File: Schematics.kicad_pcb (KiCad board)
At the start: 2 copper layers, 73 parts, among them Q1 AO3400A, Q2 SI2301CDS-T1-E3, Q3 SI2301CDS-T1-E3, Q4 8050, U2 CAT24C32, U3 ME6217C33M5G, U6 TXB0108PWR

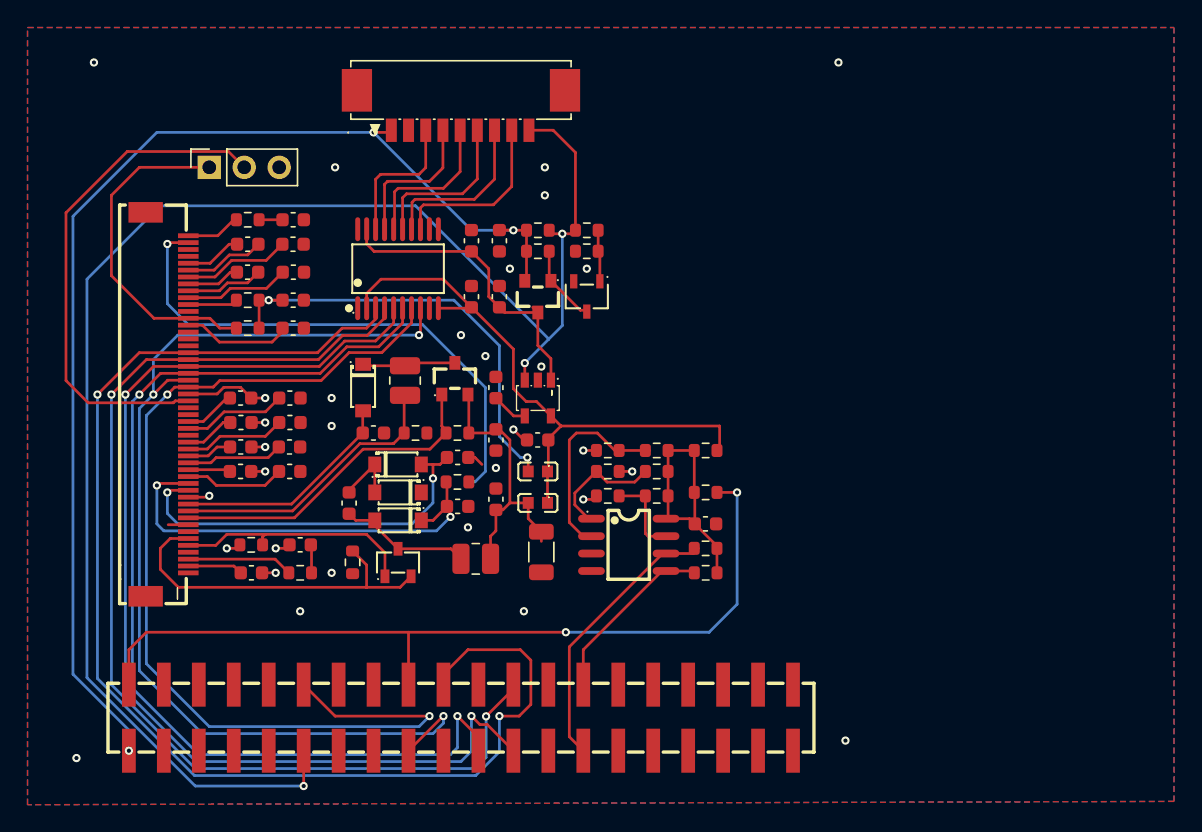
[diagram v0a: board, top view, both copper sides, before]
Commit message: made changes to simplify the board
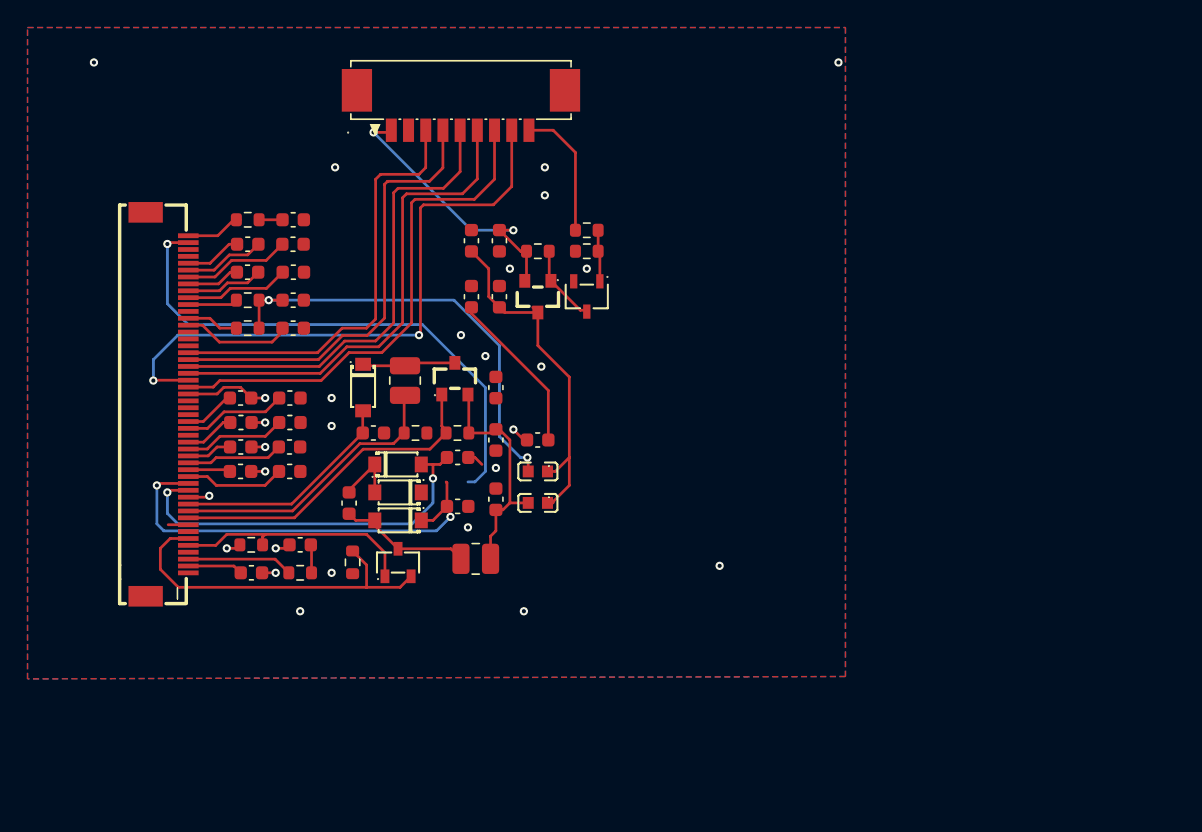
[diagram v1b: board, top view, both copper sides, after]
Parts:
- removed C23: 100nF/50V, Capacitor_SMD:C_0603_1608Metric
- removed C29: 100uF/6.3V, Capacitor_SMD:C_1206_3216Metric
- removed J2: ~, Connector_PinSocket_2.54mm:PinSocket_1x03_P2.54mm_Vertical
- removed R1, R16, R17, R19: 0R, Resistor_SMD:R_0603_1608Metric
- removed R10, R14, R18, R9: NC, Resistor_SMD:R_0603_1608Metric
- removed R12: 1K, Resistor_SMD:R_0603_1608Metric
- removed R13, R15: 3.9KΩ, Resistor_SMD:R_0603_1608Metric
- removed R7: NC/47K, Resistor_SMD:R_0603_1608Metric
- removed U2: CAT24C32, local:SOIC-8_L5.0-W4.0-P1.27-LS6.0-BL
- removed U3: ME6217C33M5G, local:SOT-23-5_L3.0-W1.7-P0.95-LS2.8-BR
- removed U6: TXB0108PWR, local:TSSOP-20_L6.5-W4.4-P0.65-LS6.4-BL
- removed UP1: ~, local:HDR-SMD_40P-P2.54-V-F-R2-C20-S2.54-LS7.1
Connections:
- net /RPI_5V renamed /VCC_INT
- net VDD renamed /VDD
- J1 pad 26: /BS0 -> GND
- J1 pad 28: /EPD_RST' -> /EPD_RST
- J1 pad 29: /EPD_BUSY' -> /EPD_BUSY
- J1 pad 30: /EPD_DC' -> /EPD_DC
- J1 pad 31: /EPD_CS' -> /EPD_CS
- J1 pad 32: /EPD_SCK' -> /EPD_SCK
- J1 pad 33: /EPD_DIN' -> /EPD_DIN
- L3 pad 1: 3V3_OUT -> VCC
- L4 pad 1: 3V3_OUT -> VCC
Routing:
- net /PWR: track 113.9 -> 10.1 mm, vias 3 -> 0
- net /EPD_DIN': track 93.4 -> 0.00 mm, vias 2 -> 0
- net /EPD_SCK': track 80.3 -> 0.00 mm, vias 2 -> 0
- net /EPD_CS': track 78.5 -> 0.00 mm, vias 2 -> 0
- net /EPD_BUSY': track 76.4 -> 0.00 mm, vias 3 -> 0
- net /EPD_DC': track 75.2 -> 0.00 mm, vias 2 -> 0
- net /EPD_RST': track 74.0 -> 0.00 mm, vias 2 -> 0
- net /VCC_INT: track 85.1 -> 20.3 mm, vias 3 -> 2
- net /RPI_3V3: track 61.3 -> 0.00 mm, vias 2 -> 0
- net /BS0: track 37.1 -> 0.00 mm
- net /EPD_BUSY: track 12.9 -> 44.8 mm, vias 0 -> 2
- net 3V3_OUT: track 43.6 -> 12.0 mm
- net /EPD_RST: track 12.2 -> 37.2 mm
- net /EPD_DC: track 11.8 -> 35.7 mm
- net /EPD_CS: track 11.1 -> 34.2 mm
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
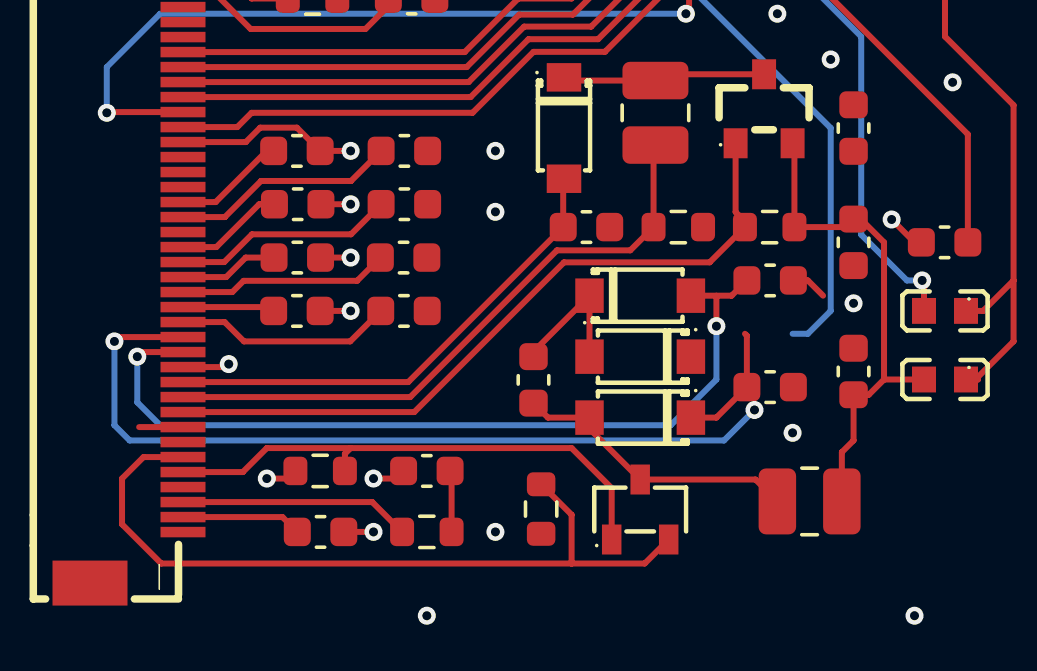
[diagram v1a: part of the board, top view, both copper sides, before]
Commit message: updated board by removing unnecessary elements
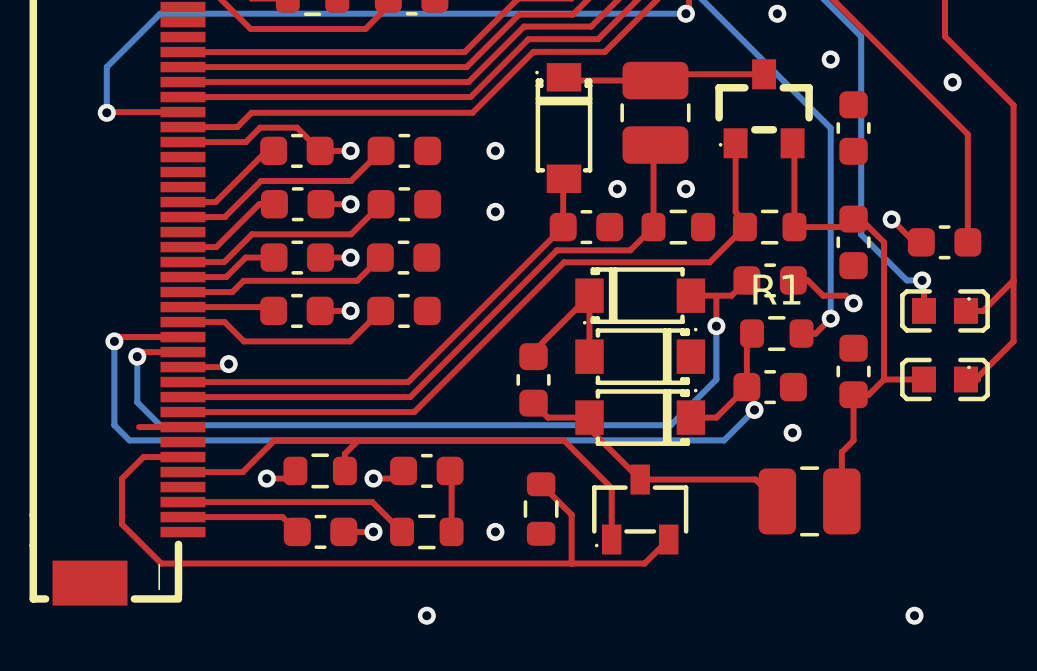
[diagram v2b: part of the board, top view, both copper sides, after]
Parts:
- added R1: 0R, Resistor_SMD:R_0603_1608Metric, F.Cu at (80.2, 66.5)
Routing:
- net GND: track 17.8 -> 18.9 mm, vias 27 -> 29
- net /GDRH: track 17.7 -> 18.3 mm
- net /VGH: track 39.2 -> 38.8 mm, vias 1 -> 2
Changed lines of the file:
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@@
 		)
 	)
+	(footprint "Resistor_SMD:R_0603_1608Metric"
+		(layer "F.Cu")
+		(at 80.245 66.541)
+		(descr "Resistor SMD 0603 (1608 Metric), square (rectangular) end terminal, IPC-7351 nominal, (Body size source: IPC-SM-782 page 72, https://www.pcb-3d.com/wordpress/wp-content/uploads/ipc-sm-782a_amendment_1_and_2.pdf)")
+		(tags "resistor")
+		(property "Reference" "R1"
+			(at 0 -1.43 0)
+			(layer "F.SilkS")
+			(effects
+				(font
+					(size 1 1)
+					(thickness 0.15)
+				)
+			)
+		)
+		(property "Value" "0R"
+			(at 0 1.43 0)
+			(layer "F.Fab")
+			(effects
+				(font
+					(size 1 1)
+					(thickness 0.15)
+				)
+			)
+		)
+		(property "Datasheet" ""
+			(at 0 0 0)
+			(layer "F.Fab")
+			(hide yes)
+			(effects
+				(font
+					(size 1.27 1.27)
+				)
+			)
+		)
+		(property "Description" "Resistor, small symbol"
+			(at 0 0 0)
+			(layer "F.Fab")
+			(hide yes)
+			(effects
+				(font
+					(size 1.27 1.27)
+				)
+			)
+		)
+		(property "KiLib_Generator" "SMD_2terminal_chip_molded"
+			(at 0 0 0)
+			(layer "F.SilkS")
+			(hide yes)
+			(effects
+				(font
+					(size 1 1)
+					(thickness 0.15)
+				)
+			)
+		)
+		(property ki_fp_filters "R_*")
+		(sheetname "/")
+		(sheetfile "Schematics.kicad_sch")
+		(units
+			(unit
+				(name "A")
+				(pins "1" "2")
+			)
+		)
+		(attr smd)
+		(duplicate_pad_numbers_are_jumpers no)
+		(fp_line
+			(start -0.237258 -0.5225)
+			(end 0.237258 -0.5225)
+			(stroke
+				(width 0.12)
+				(type solid)
+			)
+			(layer "F.SilkS")
+		)
+		(fp_line
+			(start -0.237258 0.5225)
+			(end 0.237258 0.5225)
+			(stroke
+				(width 0.12)
+				(type solid)
+			)
+			(layer "F.SilkS")
+		)
+		(fp_rect
+			(start -1.48 -0.73)
+			(end 1.48 0.73)
+			(stroke
+				(width 0.05)
+				(type solid)
+			)
+			(fill no)
+			(layer "F.CrtYd")
+		)
+		(fp_rect
+			(start -0.8 -0.4125)
+			(end 0.8 0.4125)
+			(stroke
+				(width 0.1)
+				(type solid)
+			)
+			(fill no)
+			(layer "F.Fab")
+		)
+		(fp_text user "${REFERENCE}"
+			(at 0 0 0)
+			(layer "F.Fab")
+			(effects
+				(font
+					(size 0.4 0.4)
+					(thickness 0.06)
+				)
+			)
+		)
+		(pad "1" smd roundrect
+			(at -0.825 0)
+			(size 0.8 0.95)
+			(layers "F.Cu" "F.Mask" "F.Paste")
+			(roundrect_rratio 0.25)
+			(net "/VPH")
+			(pintype "passive")
+		)
+		(pad "2" smd roundrect
+			(at 0.825 0)
+			(size 0.8 0.95)
+			(layers "F.Cu" "F.Mask" "F.Paste")
+			(roundrect_rratio 0.25)
+			(net "/VGH")
+			(pintype "passive")
+		)
+		(embedded_fonts no)
+		(model "${KICAD10_3DMODEL_DIR}/Resistor_SMD.3dshapes/R_0603_1608Metric.step"
+			(offset
+				(xyz 0 0 0)
+			)
+			(scale
+				(xyz 1 1 1)
+			)
+			(rotate
+				(xyz 0 0 0)
+			)
+		)
+	)
 	(footprint "local:SOD-123_L2.8-W1.8-LS3.7-RD"
 		(layer "F.Cu")
@@
 	)
 	(segment
+		(start 82.55 65.278)
+		(end 82.804 65.532)
+		(width 0.2)
+		(layer "F.Cu")
+		(net "GND")
+	)
+	(segment
 		(start 65.812 73.152)
 		(end 66.802 73.152)
@@
 	)
 	(segment
+		(start 81.788 65.278)
+		(end 82.55 65.278)
+		(width 0.2)
+		(layer "F.Cu")
+		(net "GND")
+	)
+	(segment
 		(start 67.551 71.374)
 		(end 67.805 71.12)
@@
 	)
 	(via
+		(at 74.93 61.722)
+		(size 0.6)
+		(drill 0.3)
+		(layers "F.Cu" "B.Cu")
+		(free yes)
+		(net "GND")
+	)
+	(via
 		(at 63.246 71.374)
 		(size 0.6)
@@
 	)
 	(via
+		(at 77.216 61.722)
+		(size 0.6)
+		(drill 0.3)
+		(layers "F.Cu" "B.Cu")
+		(free yes)
+		(net "GND")
+	)
+	(via
 		(at 86.106 58.166)
 		(size 0.6)
@@
 	)
 	(segment
-		(start 63.246 70.358)
-		(end 62.446 71.158)
+		(start 65.849 71.12)
+		(end 65.849 70.553)
 		(width 0.2)
 		(layer "F.Cu")
@@
 	)
 	(segment
-		(start 66.04 70.358)
-		(end 63.246 70.358)
+		(start 63.5 70.104)
+		(end 66.294 70.104)
 		(width 0.2)
 		(layer "F.Cu")
@@
 	)
 	(segment
-		(start 74.742 73.406)
-		(end 74.742 71.694)
+		(start 62.446 71.158)
+		(end 63.5 70.104)
 		(width 0.2)
 		(layer "F.Cu")
@@
 	)
 	(segment
-		(start 65.847 70.551)
-		(end 66.04 70.358)
+		(start 74.742 71.694)
+		(end 73.152 70.104)
 		(width 0.2)
 		(layer "F.Cu")
@@
 	)
 	(segment
-		(start 65.849 70.553)
-		(end 65.849 71.12)
+		(start 60.452 71.158)
+		(end 62.446 71.158)
 		(width 0.2)
 		(layer "F.Cu")
@@
 	)
 	(segment
-		(start 65.847 70.551)
-		(end 65.849 70.553)
+		(start 65.849 70.553)
+		(end 65.847 70.551)
 		(width 0.2)
 		(layer "F.Cu")
@@
 	)
 	(segment
-		(start 74.742 71.694)
-		(end 73.406 70.358)
+		(start 65.847 70.551)
+		(end 66.294 70.104)
 		(width 0.2)
 		(layer "F.Cu")
@@
 	)
 	(segment
-		(start 73.406 70.358)
-		(end 66.04 70.358)
+		(start 74.742 73.406)
+		(end 74.742 71.694)
 		(width 0.2)
 		(layer "F.Cu")
@@
 	)
 	(segment
-		(start 62.446 71.158)
-		(end 60.452 71.158)
+		(start 66.294 70.104)
+		(end 73.152 70.104)
 		(width 0.2)
 		(layer "F.Cu")
@@
 	)
 	(segment
+		(start 81.541 66.541)
+		(end 82.042 66.04)
+		(width 0.2)
+		(layer "F.Cu")
+		(net "/VGH")
+	)
+	(segment
 		(start 59.028 49.158)
 		(end 60.452 49.158)
@@
 		(net "/VGH")
 	)
+	(segment
+		(start 81.07 66.541)
+		(end 81.541 66.541)
+		(width 0.2)
+		(layer "F.Cu")
+		(net "/VGH")
+	)
+	(via
+		(at 82.042 66.04)
+		(size 0.6)
+		(drill 0.3)
+		(layers "F.Cu" "B.Cu")
+		(net "/VGH")
+	)
 	(via
 		(at 58.928 49.258)
@@
 	)
 	(segment
-		(start 81.28 66.548)
-		(end 80.772 66.548)
-		(width 0.2)
-		(layer "B.Cu")
-		(net "/VGH")
-	)
-	(segment
 		(start 77.47 55.118)
 		(end 82.042 59.69)
@@
 	)
 	(segment
-		(start 82.042 65.786)
-		(end 81.28 66.548)
-		(width 0.2)
-		(layer "B.Cu")
-		(net "/VGH")
-	)
-	(segment
 		(start 58.928 53.594)
 		(end 60.452 55.118)
@@
 		)
 		(min_thickness 0.25)
-		(fill
+		(fill yes
 			(thermal_gap 0.5)
 			(thermal_bridge_width 0.5)

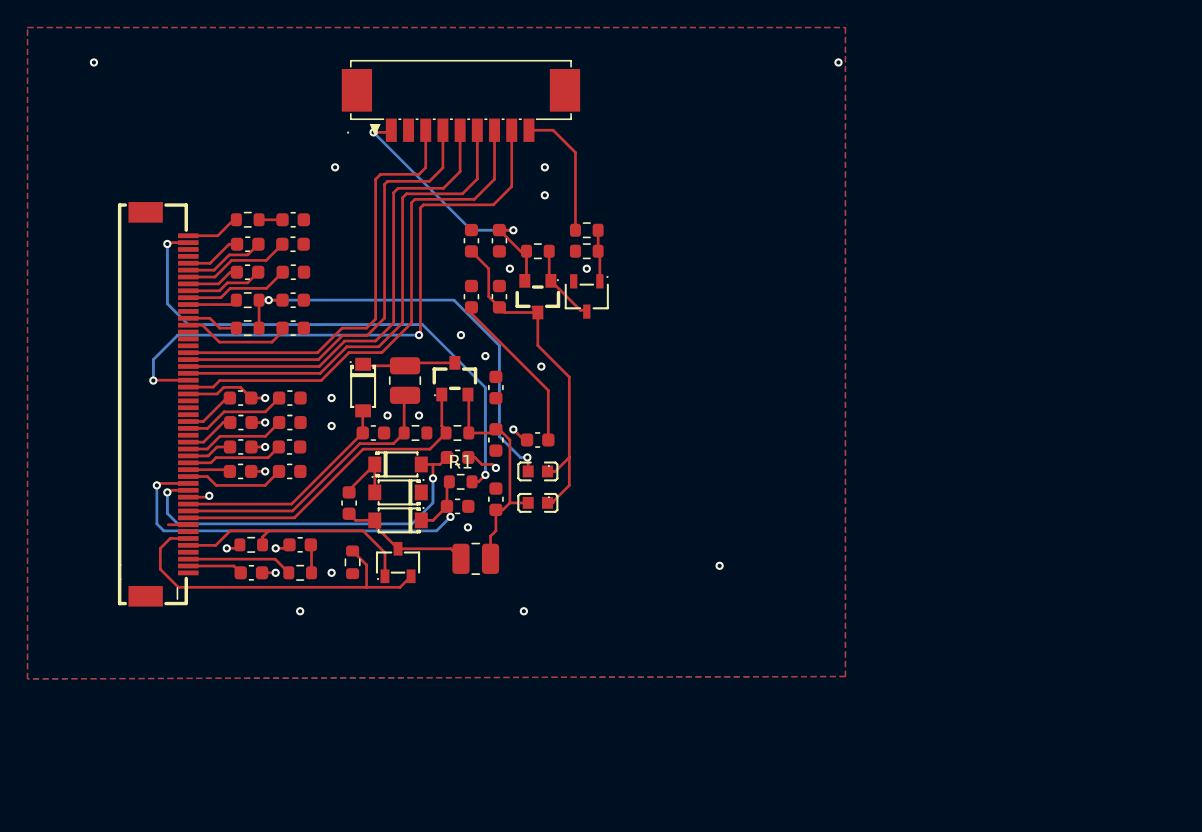
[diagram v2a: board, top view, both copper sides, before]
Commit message: completed minimalist schematics and PCB of epaper
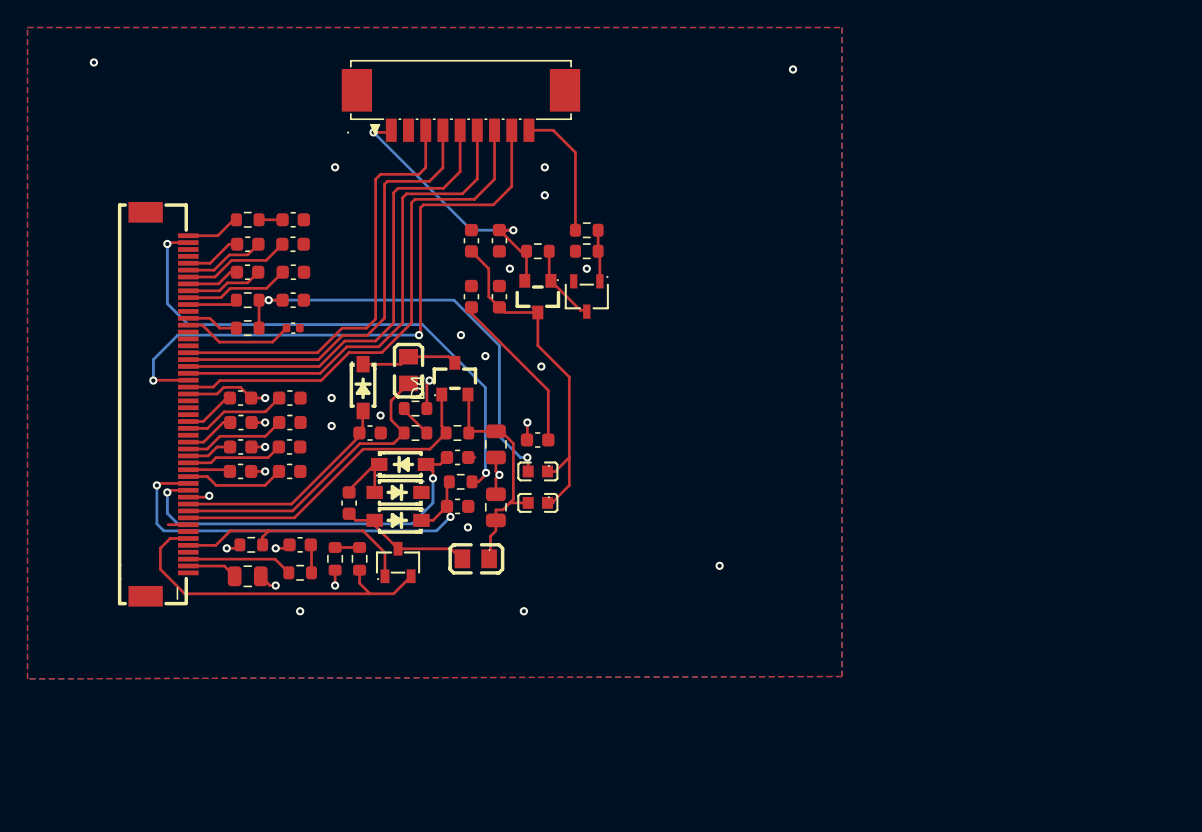
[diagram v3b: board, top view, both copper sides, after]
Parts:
- removed C28: NC, Capacitor_SMD:C_0603_1608Metric
- added R7: 0.1Ω, Resistor_SMD:R_0603_1608Metric, F.Cu at (71.1, 72.1)
- added R9: 0.1Ω, Resistor_SMD:R_0603_1608Metric, F.Cu at (77.0, 63.0)
- C1, C13, C5: footprint Capacitor_SMD:C_0603_1608Metric -> Capacitor_SMD:C_0805_2012Metric
- C14: footprint Capacitor_SMD:C_0603_1608Metric -> Capacitor_SMD:C_0402_1005Metric
- D1, D2, D3, D4: footprint local:SOD-123_L2.8-W1.8-LS3.7-RD -> local:SOD-123_L2.7-W1.6-LS3.7-RD-1
- L1, L2: footprint Inductor_SMD:L_1008_2520Metric -> local:L0805
- R3, R5: value 0.2Ω -> 0.1Ω
- moved R5 1.78 mm to (77.0, 61.2)
- moved L2 0.80 mm to (76.5, 58.4)
- moved C5 0.59 mm to (82.8, 68.4)
- moved R3 0.57 mm to (72.9, 72.1), turned to -90 degrees
- moved C1 0.37 mm to (64.8, 73.4)
- moved D2 0.33 mm to (76.0, 65.3)
- moved C13 0.32 mm to (82.8, 63.8)
- moved C16 0.24 mm to (73.7, 63.0)
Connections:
- R3 pad 1: GND -> Net-(R3-Pad1)
- R5 pad 1: /RESEC -> Net-(R5-Pad1)
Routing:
- net GND: track 18.9 -> 23.1 mm
- net Net-(R5-Pad1): track 0.00 -> 2.46 mm
- net Net-(R3-Pad1): track 0.00 -> 1.78 mm
- net /RESEC: track 21.1 -> 22.6 mm
- net /RESEH: track 26.0 -> 25.4 mm
